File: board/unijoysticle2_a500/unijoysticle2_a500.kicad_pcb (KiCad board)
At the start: 4 copper layers, 67 x 52 mm, 55 parts, among them J1 USB_B_Micro, J2 PORT JOY #1, J3 PORT JOY #2, Q1 S8050, Q2 S8050, SW1 RESET, SW2 BOOT, SW3 MOUSE, SW4 SWAP, U1 ESP32-WROOM-32E, U2 AMS1117-3.3, U3 CH340C, U4 74HC05, U5 74HC05, U6 74HC05

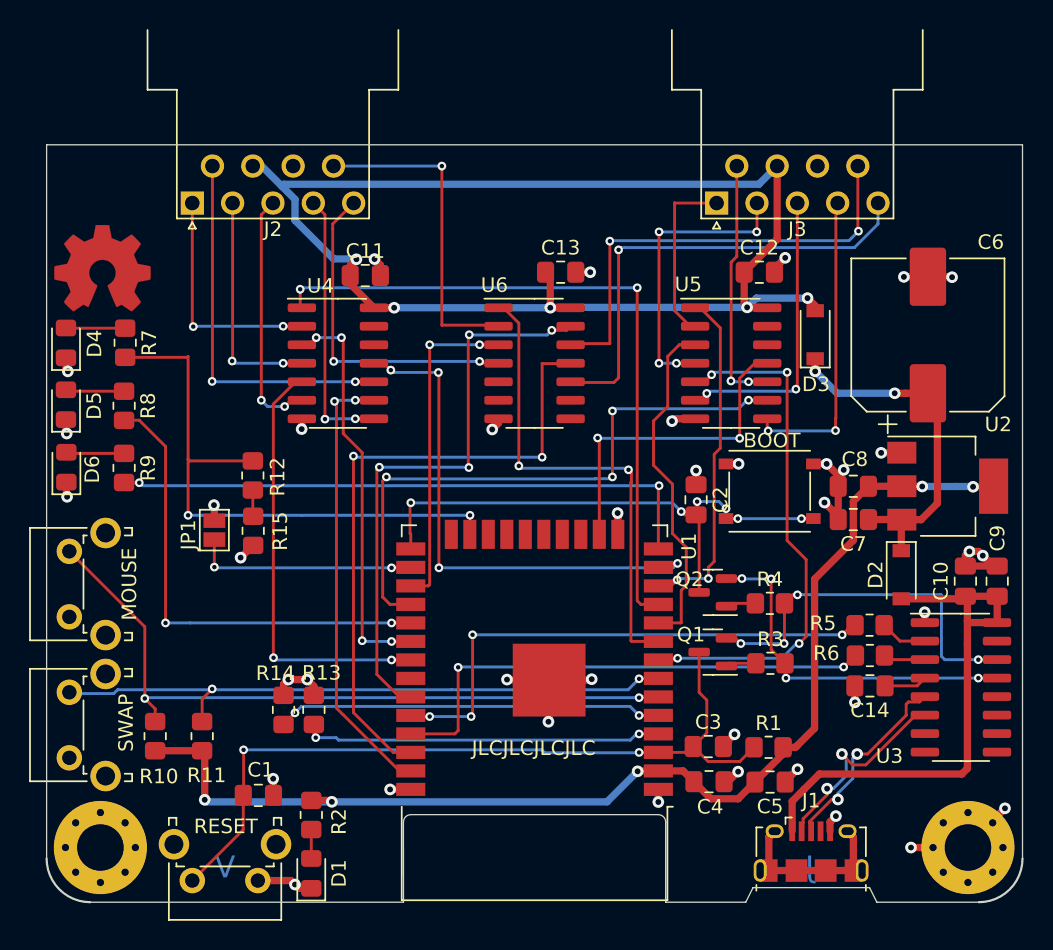
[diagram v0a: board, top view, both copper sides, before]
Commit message: uni2 a500: revert CH340 from 5V
Autoreset is driven by DTS/RTS.
But if DTS/RTS are not used (requires that CH340 is powered) then
autoreset doesn't work.
So, although we shouldn't power CH340 when it is powered from the Amiga,
since it consumes current, we need it for autoreset.

Besides, we don't gain much by not powering CH340. Only 0.02 amps
according to my measures.
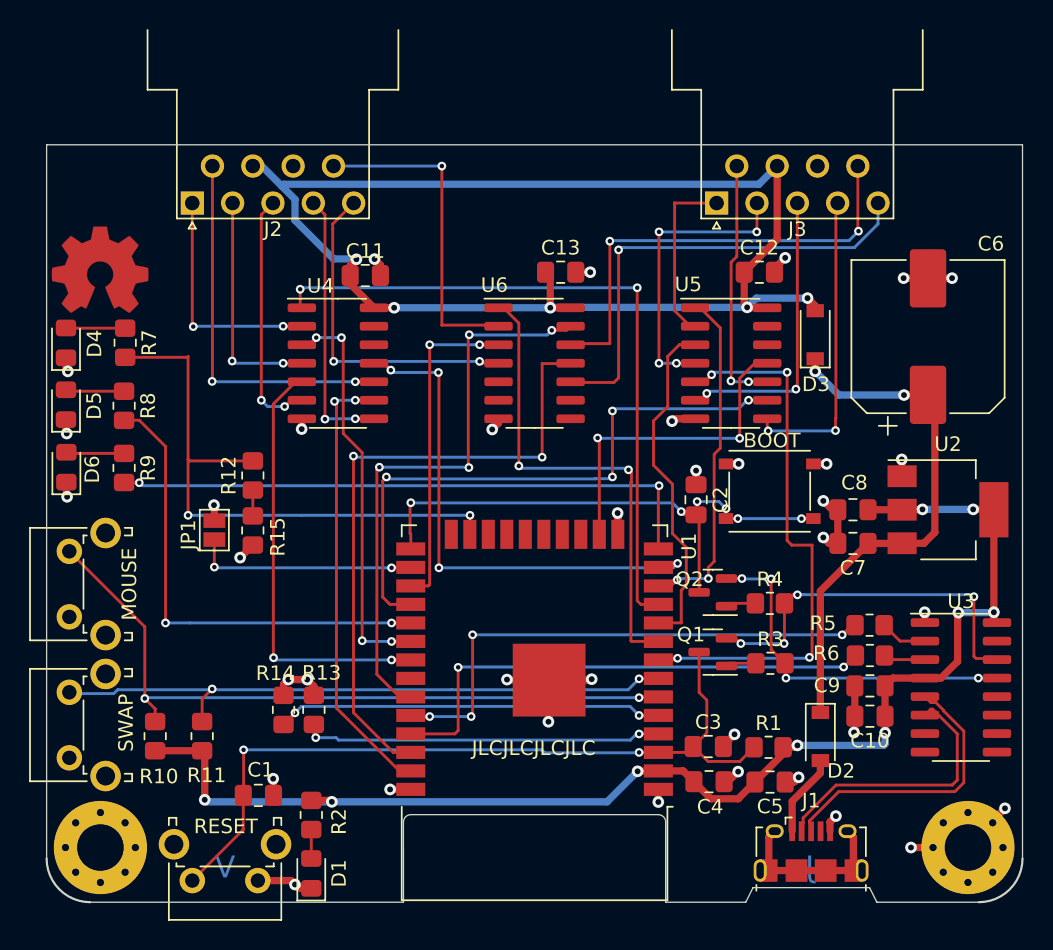
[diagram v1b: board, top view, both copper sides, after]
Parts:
- removed C14: .1uF, Capacitor_SMD:C_0805_2012Metric_Pad1.18x1.45mm_HandSolder
- R12, R2, R7, R8, R9: value 2.2K -> 3.3K
- moved D2 12.4 mm to (133.1, 136.6)
- moved C10 11.4 mm to (136.5, 135.2), turned to 180 degrees
- moved C9 11.3 mm to (136.5, 133.1), turned to 180 degrees
- moved C7 1.64 mm to (135.4, 123.4)
- moved U2 1.62 mm to (141.9, 121.1)
- moved C8 1.61 mm to (135.4, 121.1)
- moved REF** 0.19 mm to (83.7, 104.6)
- moved C6 0.11 mm to (140.5, 109.2)
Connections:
- C10 pad 1: VBUS -> +3V3
- C9 pad 1: VBUS -> +3V3
- U3 pad 16: VBUS -> +3V3
- U3 pad 4: Net-(U3-Pad4) -> +3V3
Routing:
- net VBUS: track 37.5 -> 5.65 mm
- net Net-(C6-Pad1): track 24.4 -> 36.8 mm
- net +3V3: track 81.0 -> 90.6 mm, vias 5 -> 9
- net /USB Serial & Power/USBD+: track 13.7 -> 19.6 mm, vias 2 -> 0
- net GND: track 65.6 -> 60.1 mm, vias 39 -> 37
- net /USB Serial & Power/USBD-: track 14.4 -> 18.9 mm, vias 2 -> 0
- net Net-(U3-Pad4): track 2.96 -> 0.00 mm
- net GPIO_J2_LEFT: track 36.1 -> 38.2 mm
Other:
- board text added: "Unijoysticle 2 A500 Rev. C"
- board text removed: "Unijoysticle 2 A500 Rev. B"

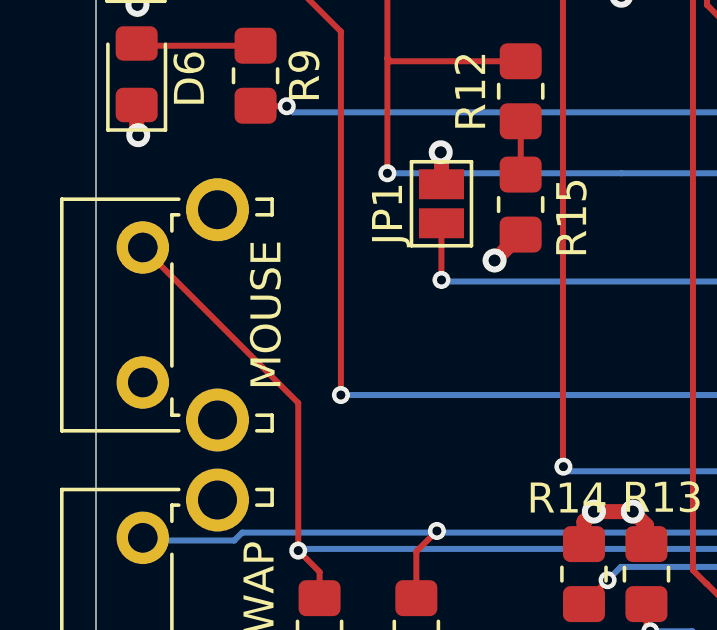
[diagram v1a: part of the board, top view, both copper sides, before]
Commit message: uni2 a500: silkscreen improments
mouse -> mode
add copyright
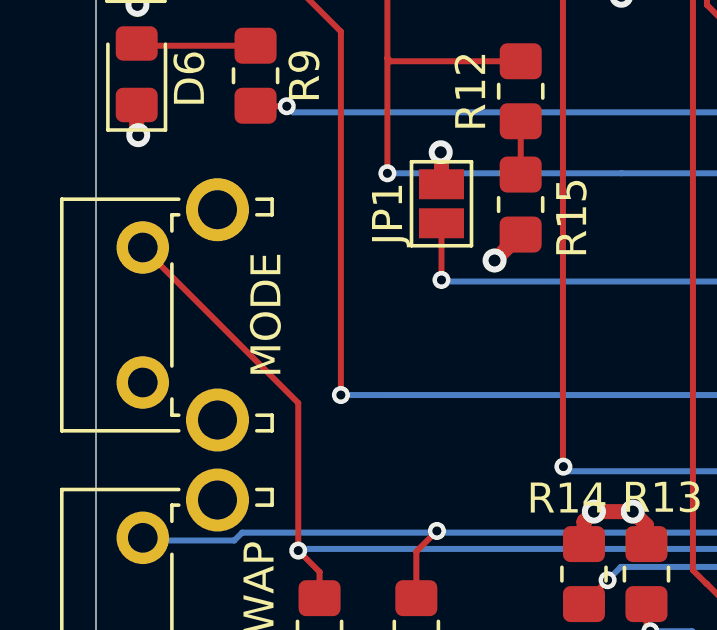
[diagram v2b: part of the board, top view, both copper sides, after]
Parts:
- SW3: value MOUSE -> MODE
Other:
- board text added: "©️ 2022 Ricardo Quesada http://retro.moe"
- board text removed: "http://retro.moe"
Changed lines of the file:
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@@
       (effects (font (size 1 1) (thickness 0.15)))
     )
-    (fp_text value "MOUSE" (at 2.25 4.1229 90) (layer "F.SilkS")
+    (fp_text value "MODE" (at 2.25 4.1229 90) (layer "F.SilkS")
       (effects (font (size 1 1) (thickness 0.15)))
     )
@@
     (effects (font (size 1.5 1.5) (thickness 0.3)) (justify mirror))
   )
-  (gr_text "Unijoysticle 2 A500\nRev. C" (at 113.62 131.185) (layer "B.SilkS")
+  (gr_text "Unijoysticle 2 A500\nRev. C" (at 113.615 130.73) (layer "B.SilkS")
     (effects (font (size 1.5 1.5) (thickness 0.3)) (justify mirror))
   )
-  (gr_text "http://retro.moe" (at 113.5634 139.3698) (layer "B.SilkS")
-    (effects (font (size 1.7 1.7) (thickness 0.2)) (justify mirror))
+  (gr_text "©️ 2022 Ricardo Quesada\nhttp://retro.moe" (at 113.5634 138.75) (layer "B.SilkS")
+    (effects (font (size 1.5 1.5) (thickness 0.2)) (justify mirror))
   )
   (gr_text "JLCJLCJLCJLC" (at 113.435 137.43) (layer "F.SilkS")
